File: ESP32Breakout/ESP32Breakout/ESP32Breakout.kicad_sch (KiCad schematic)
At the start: 10 parts, among them J1 Conn_01x14_Socket, J2 Conn_01x14_Socket, J3 5V INPUT, J4 Bell Power, J5 Relay Out 1, J6 Relay Out 2, K1 G5V-2_Split, Q1 BSS214NW

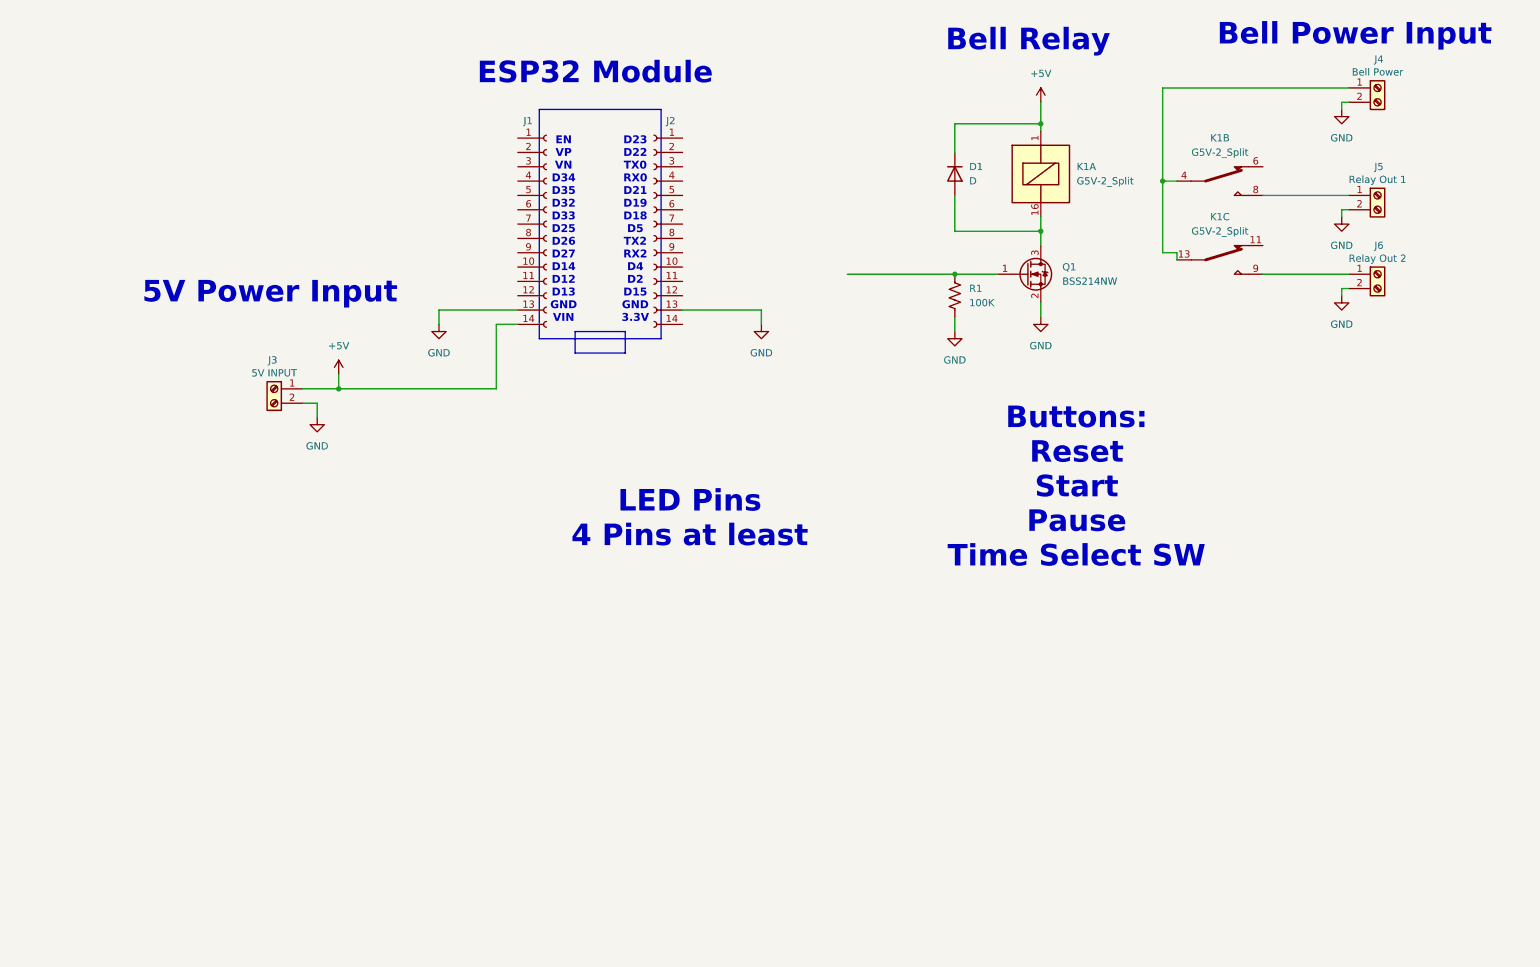
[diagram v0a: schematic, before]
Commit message: finished routing and DRC cleanup
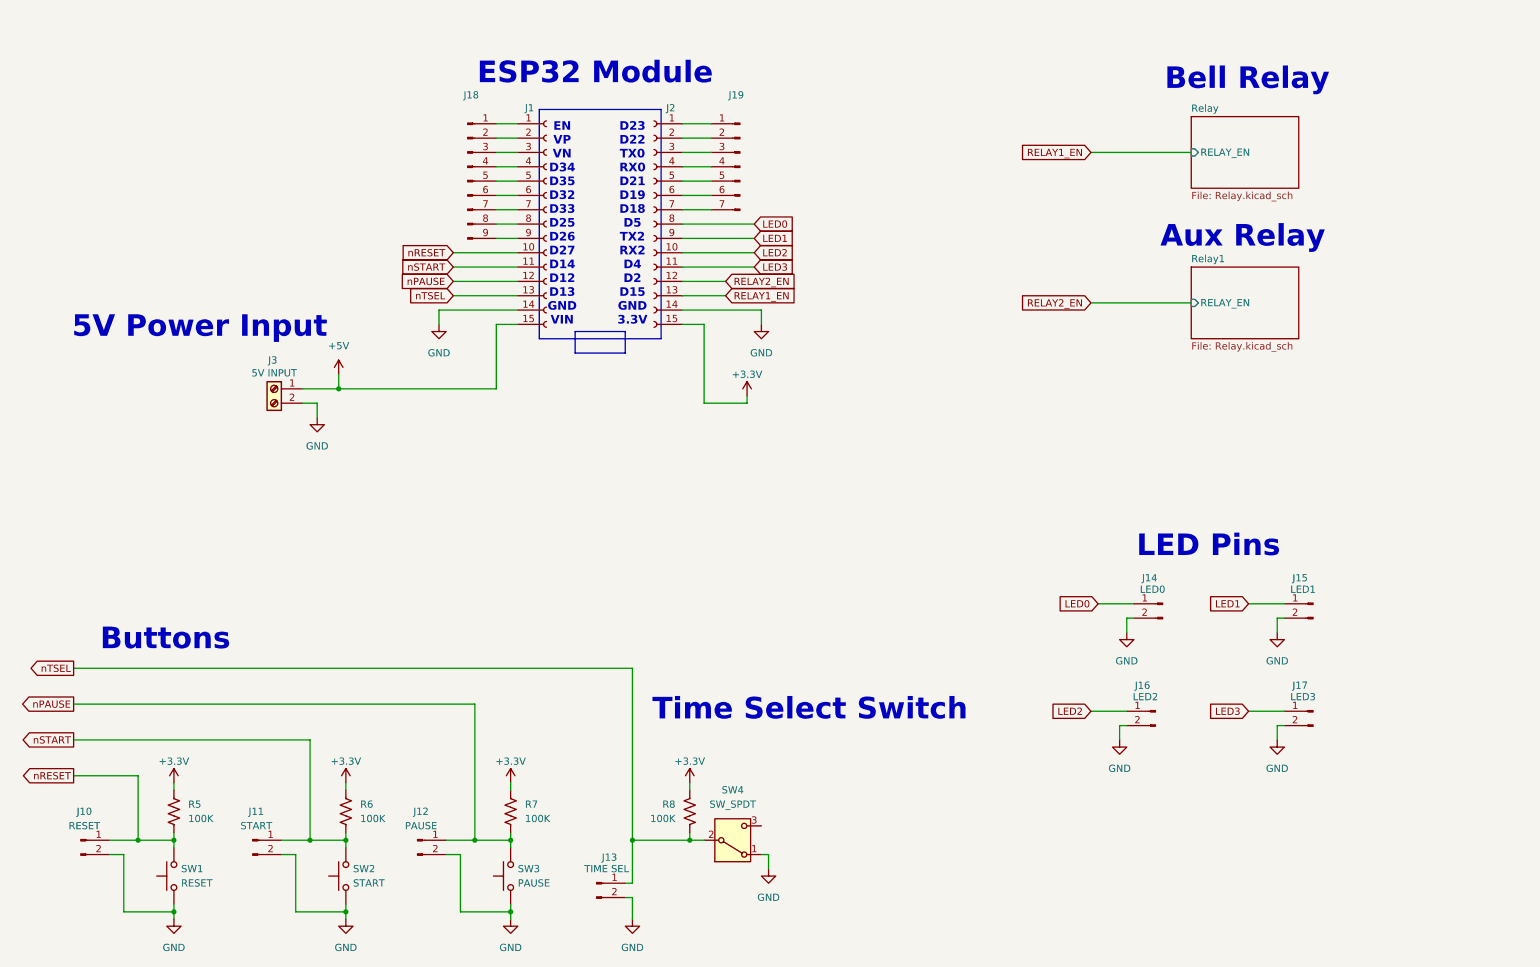
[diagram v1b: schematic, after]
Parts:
- removed D1: D, symbol Device:D
- removed J1, J2: Conn_01x14_Socket, symbol Connector:Conn_01x14_Socket
- removed J4: Bell Power, symbol Connector:Screw_Terminal_01x02
- removed J5: Relay Out 1, symbol Connector:Screw_Terminal_01x02
- removed J6: Relay Out 2, symbol Connector:Screw_Terminal_01x02
- removed K1: G5V-2_Split, Relay_THT:Relay_DPDT_Omron_G5V-2, symbol Relay:G5V-2_Split
- removed Q1: BSS214NW, Package_TO_SOT_SMD:SOT-323_SC-70, symbol Transistor_FET:BSS214NW
- removed R1: 100K, symbol Device:R_US
- added J1, J2: Conn_01x15_Socket, Connector_PinHeader_2.54mm:PinHeader_1x15_P2.54mm_Vertical, symbol Connector:Conn_01x15_Socket
- added J10: RESET, Connector_PinHeader_2.54mm:PinHeader_1x02_P2.54mm_Vertical, symbol Connector:Conn_01x02_Pin
- added J11: START, Connector_PinHeader_2.54mm:PinHeader_1x02_P2.54mm_Vertical, symbol Connector:Conn_01x02_Pin
- added J12: PAUSE, Connector_PinHeader_2.54mm:PinHeader_1x02_P2.54mm_Vertical, symbol Connector:Conn_01x02_Pin
- added J13: TIME SEL, Connector_PinHeader_2.54mm:PinHeader_1x02_P2.54mm_Vertical, symbol Connector:Conn_01x02_Pin
- added J14: LED0, Connector_PinHeader_2.54mm:PinHeader_1x02_P2.54mm_Vertical, symbol Connector:Conn_01x02_Pin
- added J15: LED1, Connector_PinHeader_2.54mm:PinHeader_1x02_P2.54mm_Vertical, symbol Connector:Conn_01x02_Pin
- added J16: LED2, Connector_PinHeader_2.54mm:PinHeader_1x02_P2.54mm_Vertical, symbol Connector:Conn_01x02_Pin
- added J17: LED3, Connector_PinHeader_2.54mm:PinHeader_1x02_P2.54mm_Vertical, symbol Connector:Conn_01x02_Pin
- added J18: Conn_01x09_Pin, Connector_PinHeader_2.54mm:PinHeader_1x09_P2.54mm_Vertical, symbol Connector:Conn_01x09_Pin
- added J19: Conn_01x07_Pin, Connector_PinHeader_2.54mm:PinHeader_1x07_P2.54mm_Vertical, symbol Connector:Conn_01x07_Pin
- added R5, R6, R7, R8: 100K, Resistor_SMD:R_0402_1005Metric, symbol Device:R_US
- added SW1: RESET, Button_Switch_THT:SW_PUSH-12mm, symbol Switch:SW_Push
- added SW2: START, Button_Switch_THT:SW_PUSH-12mm, symbol Switch:SW_Push
- added SW3: PAUSE, Button_Switch_THT:SW_PUSH-12mm, symbol Switch:SW_Push
- added SW4: SW_SPDT, Button_Switch_THT:SW_CK_JS202011AQN_DPDT_Angled, symbol Switch:SW_SPDT
- J3: footprint (none) -> TerminalBlock:TerminalBlock_bornier-2_P5.08mm; LCSC (none) -> C5142622
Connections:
- net +5V: now also J1.15 (Pin_15)
- net GND: now also J1.14 (Pin_14), J10.2 (Pin_2), J11.2 (Pin_2), J12.2 (Pin_2), J13.2 (Pin_2), J14.2 (Pin_2), J15.2 (Pin_2), J16.2 (Pin_2), J17.2 (Pin_2), J2.14 (Pin_14), SW1.1, SW2.1, SW3.1, SW4.1 (A)
- new net: J19.1 (Pin_1), J2.1 (Pin_1)
- new net: J19.2 (Pin_2), J2.2 (Pin_2)
- new net: J19.3 (Pin_3), J2.3 (Pin_3)
- new net: J19.4 (Pin_4), J2.4 (Pin_4)
- new net: J19.5 (Pin_5), J2.5 (Pin_5)
- new net: J19.6 (Pin_6), J2.6 (Pin_6)
- new net: J19.7 (Pin_7), J2.7 (Pin_7)
- new net: J1.1 (Pin_1), J18.1 (Pin_1)
- new net: J1.2 (Pin_2), J18.2 (Pin_2)
- new net: J1.3 (Pin_3), J18.3 (Pin_3)
- new net: J1.4 (Pin_4), J18.4 (Pin_4)
- new net: J1.5 (Pin_5), J18.5 (Pin_5)
- new net: J1.6 (Pin_6), J18.6 (Pin_6)
- new net: J1.7 (Pin_7), J18.7 (Pin_7)
- new net: J1.8 (Pin_8), J18.8 (Pin_8)
- new net: J1.9 (Pin_9), J18.9 (Pin_9)
- new net +3.3V: J2.15 (Pin_15), R5.1, R6.1, R7.1, R8.1
- new net LED0: J14.1 (Pin_1), J2.8 (Pin_8)
- new net LED1: J15.1 (Pin_1), J2.9 (Pin_9)
- new net LED2: J16.1 (Pin_1), J2.10 (Pin_10)
- new net LED3: J17.1 (Pin_1), J2.11 (Pin_11)
- new net RELAY1_EN: J2.13 (Pin_13)
- new net RELAY2_EN: J2.12 (Pin_12)
- new net nPAUSE: J1.12 (Pin_12), J12.1 (Pin_1), R7.2, SW3.2
- new net nRESET: J1.10 (Pin_10), J10.1 (Pin_1), R5.2, SW1.2
- new net nSTART: J1.11 (Pin_11), J11.1 (Pin_1), R6.2, SW2.2
- new net nTSEL: J1.13 (Pin_13), J13.1 (Pin_1), R8.2, SW4.2 (B)
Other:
- added sheet Relay (Relay.kicad_sch)
- added sheet Relay1 (Relay.kicad_sch)
- note added: "Aux Relay"
- note added: "Buttons"
- note added: "LED Pins"
- note added: "Time Select Switch"
- note removed: "Bell Power Input"
- note removed: "Buttons: Reset Start Pause Time Select SW"
- note removed: "LED Pins 4 Pins at least"

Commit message: update production files for both boards
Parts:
- J1, J2: LCSC (none) -> C124408
- J14, J15, J16, J17: LCSC (none) -> C124375
- SW1, SW2, SW3: LCSC (none) -> C5377619
- SW4: LCSC (none) -> C223857
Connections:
- net nPAUSE renamed nBTN3
- net nRESET renamed nBTN1
- net nSTART renamed nBTN2
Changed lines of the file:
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@@
 		)
 	)
-	(global_label "nPAUSE"
+	(global_label "nBTN3"
 		(shape output)
 		(at 25.4 148.59 180)
@@
 		)
 		(property "Intersheetrefs" "${INTERSHEET_REFS}"
-			(at 15.2182 148.59 0)
+			(at 16.4882 148.59 0)
 			(effects
 				(font
@@
 		)
 	)
-	(global_label "nRESET"
+	(global_label "nBTN1"
 		(shape input)
 		(at 92.71 68.58 180)
@@
 		)
 		(property "Intersheetrefs" "${INTERSHEET_REFS}"
-			(at 82.8307 68.58 0)
+			(at 83.7982 68.58 0)
 			(effects
 				(font
@@
 		)
 	)
-	(global_label "nPAUSE"
+	(global_label "nBTN3"
 		(shape input)
 		(at 92.71 73.66 180)
@@
 		)
 		(property "Intersheetrefs" "${INTERSHEET_REFS}"
-			(at 82.5282 73.66 0)
+			(at 83.7982 73.66 0)
 			(effects
 				(font
@@
 		)
 	)
-	(global_label "nSTART"
+	(global_label "nBTN2"
 		(shape input)
 		(at 92.71 71.12 180)
@@
 		)
 		(property "Intersheetrefs" "${INTERSHEET_REFS}"
-			(at 83.0725 71.12 0)
+			(at 83.7982 71.12 0)
 			(effects
 				(font
@@
 		)
 	)
-	(global_label "nSTART"
+	(global_label "nBTN2"
 		(shape output)
 		(at 25.4 154.94 180)
@@
 		)
 		(property "Intersheetrefs" "${INTERSHEET_REFS}"
-			(at 15.7625 154.94 0)
+			(at 16.4882 154.94 0)
 			(effects
 				(font
@@
 		)
 	)
-	(global_label "nRESET"
+	(global_label "nBTN1"
 		(shape output)
 		(at 25.4 161.29 180)
@@
 		)
 		(property "Intersheetrefs" "${INTERSHEET_REFS}"
-			(at 15.5207 161.29 0)
+			(at 16.4882 161.29 0)
 			(effects
 				(font
@@
 			)
 		)
+		(property "LCSC" "C124375"
+			(at 217.17 149.86 0)
+			(effects
+				(font
+					(size 1.27 1.27)
+				)
+				(hide yes)
+			)
+		)
 		(pin "2"
 		)
@@
 				)
 				(justify right)
+				(hide yes)
 			)
 		)
@@
 			)
 		)
+		(property "LCSC" "C5377619"
+			(at 43.18 179.07 90)
+			(effects
+				(font
+					(size 1.27 1.27)
+				)
+				(hide yes)
+			)
+		)
 		(pin "2"
 		)
@@
 				)
 				(justify right)
+				(hide yes)
 			)
 		)
@@
 		(property "Description" "Push button switch, generic, two pins"
 			(at 102.87 179.07 0)
+			(effects
+				(font
+					(size 1.27 1.27)
+				)
+				(hide yes)
+			)
+		)
+		(property "LCSC" "C5377619"
+			(at 102.87 179.07 90)
 			(effects
 				(font
@@
 			)
 		)
+		(property "LCSC" "C124408"
+			(at 128.27 63.5 0)
+			(effects
+				(font
+					(size 1.27 1.27)
+				)
+				(hide yes)
+			)
+		)
 		(pin "6"
 		)
@@
 			)
 		)
+		(property "LCSC" "C124408"
+			(at 109.22 63.5 0)
+			(effects
+				(font
+					(size 1.27 1.27)
+				)
+				(hide yes)
+			)
+		)
 		(pin "6"
 		)
@@
 				)
 				(justify right)
+				(hide yes)
 			)
 		)
@@
 		(property "Description" "Push button switch, generic, two pins"
 			(at 73.66 179.07 0)
+			(effects
+				(font
+					(size 1.27 1.27)
+				)
+				(hide yes)
+			)
+		)
+		(property "LCSC" "C5377619"
+			(at 73.66 179.07 90)
 			(effects
 				(font
@@
 			)
 		)
+		(property "LCSC" "C124375"
+			(at 218.44 130.81 0)
+			(effects
+				(font
+					(size 1.27 1.27)
+				)
+				(hide yes)
+			)
+		)
+		(property "Field6" ""
+			(at 218.44 130.81 0)
+			(effects
+				(font
+					(size 1.27 1.27)
+				)
+				(hide yes)
+			)
+		)
 		(pin "2"
 		)
@@
 			)
 		)
+		(property "LCSC" "C124375"
+			(at 245.11 149.86 0)
+			(effects
+				(font
+					(size 1.27 1.27)
+				)
+				(hide yes)
+			)
+		)
 		(pin "2"
 		)
@@
 			)
 		)
+		(property "LCSC" "C223857"
+			(at 142.24 172.72 0)
+			(effects
+				(font
+					(size 1.27 1.27)
+				)
+				(hide yes)
+			)
+		)
 		(pin "1"
 		)
@@
 			(at 245.11 130.81 0)
 			(effects
+				(font
+					(size 1.27 1.27)
+				)
+				(hide yes)
+			)
+		)
+		(property "LCSC" "C124375"
+			(at 245.11 130.81 0)
+			(effects
